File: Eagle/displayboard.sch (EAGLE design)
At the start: 47 parts

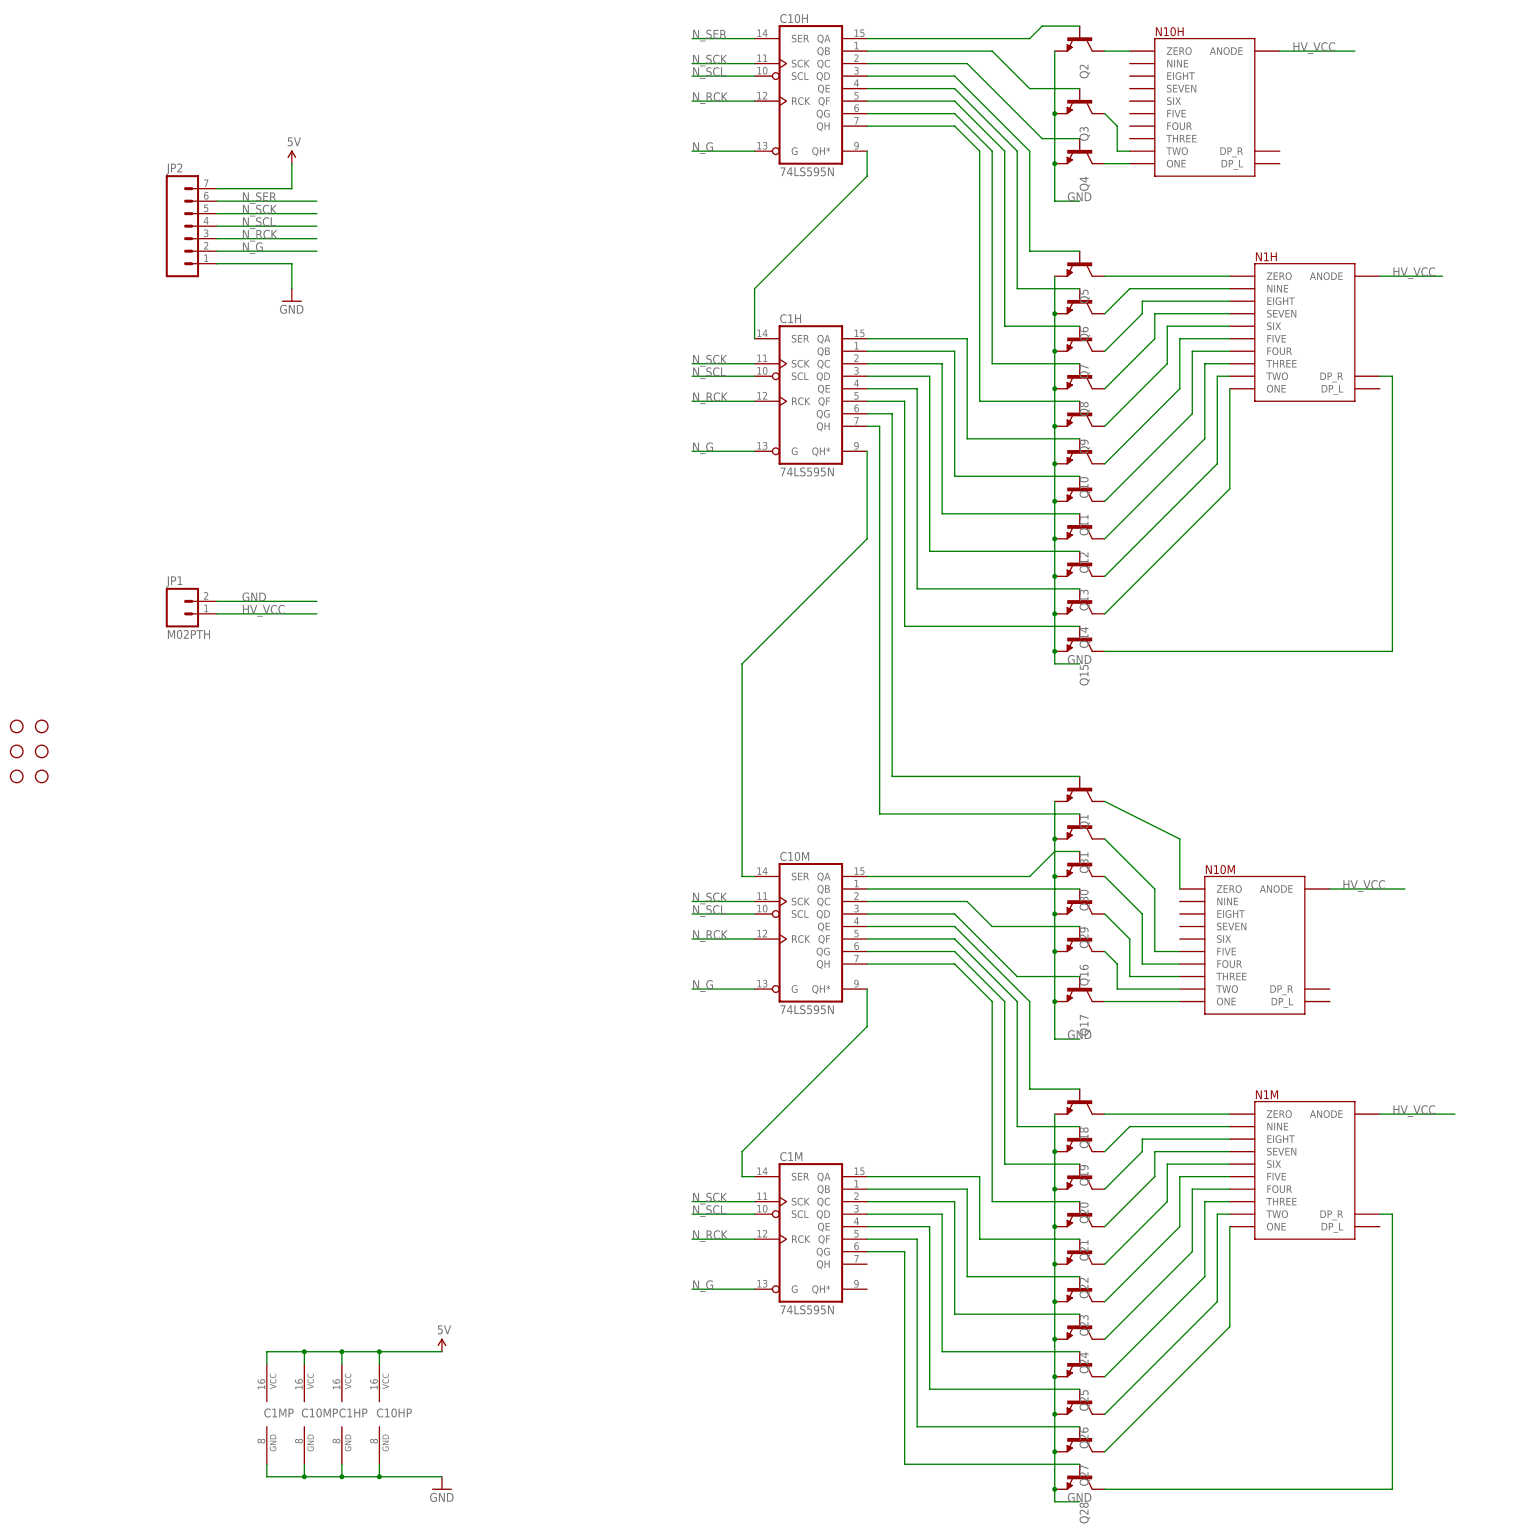
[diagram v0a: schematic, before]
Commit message: Update schematic to include on-board 200V psu
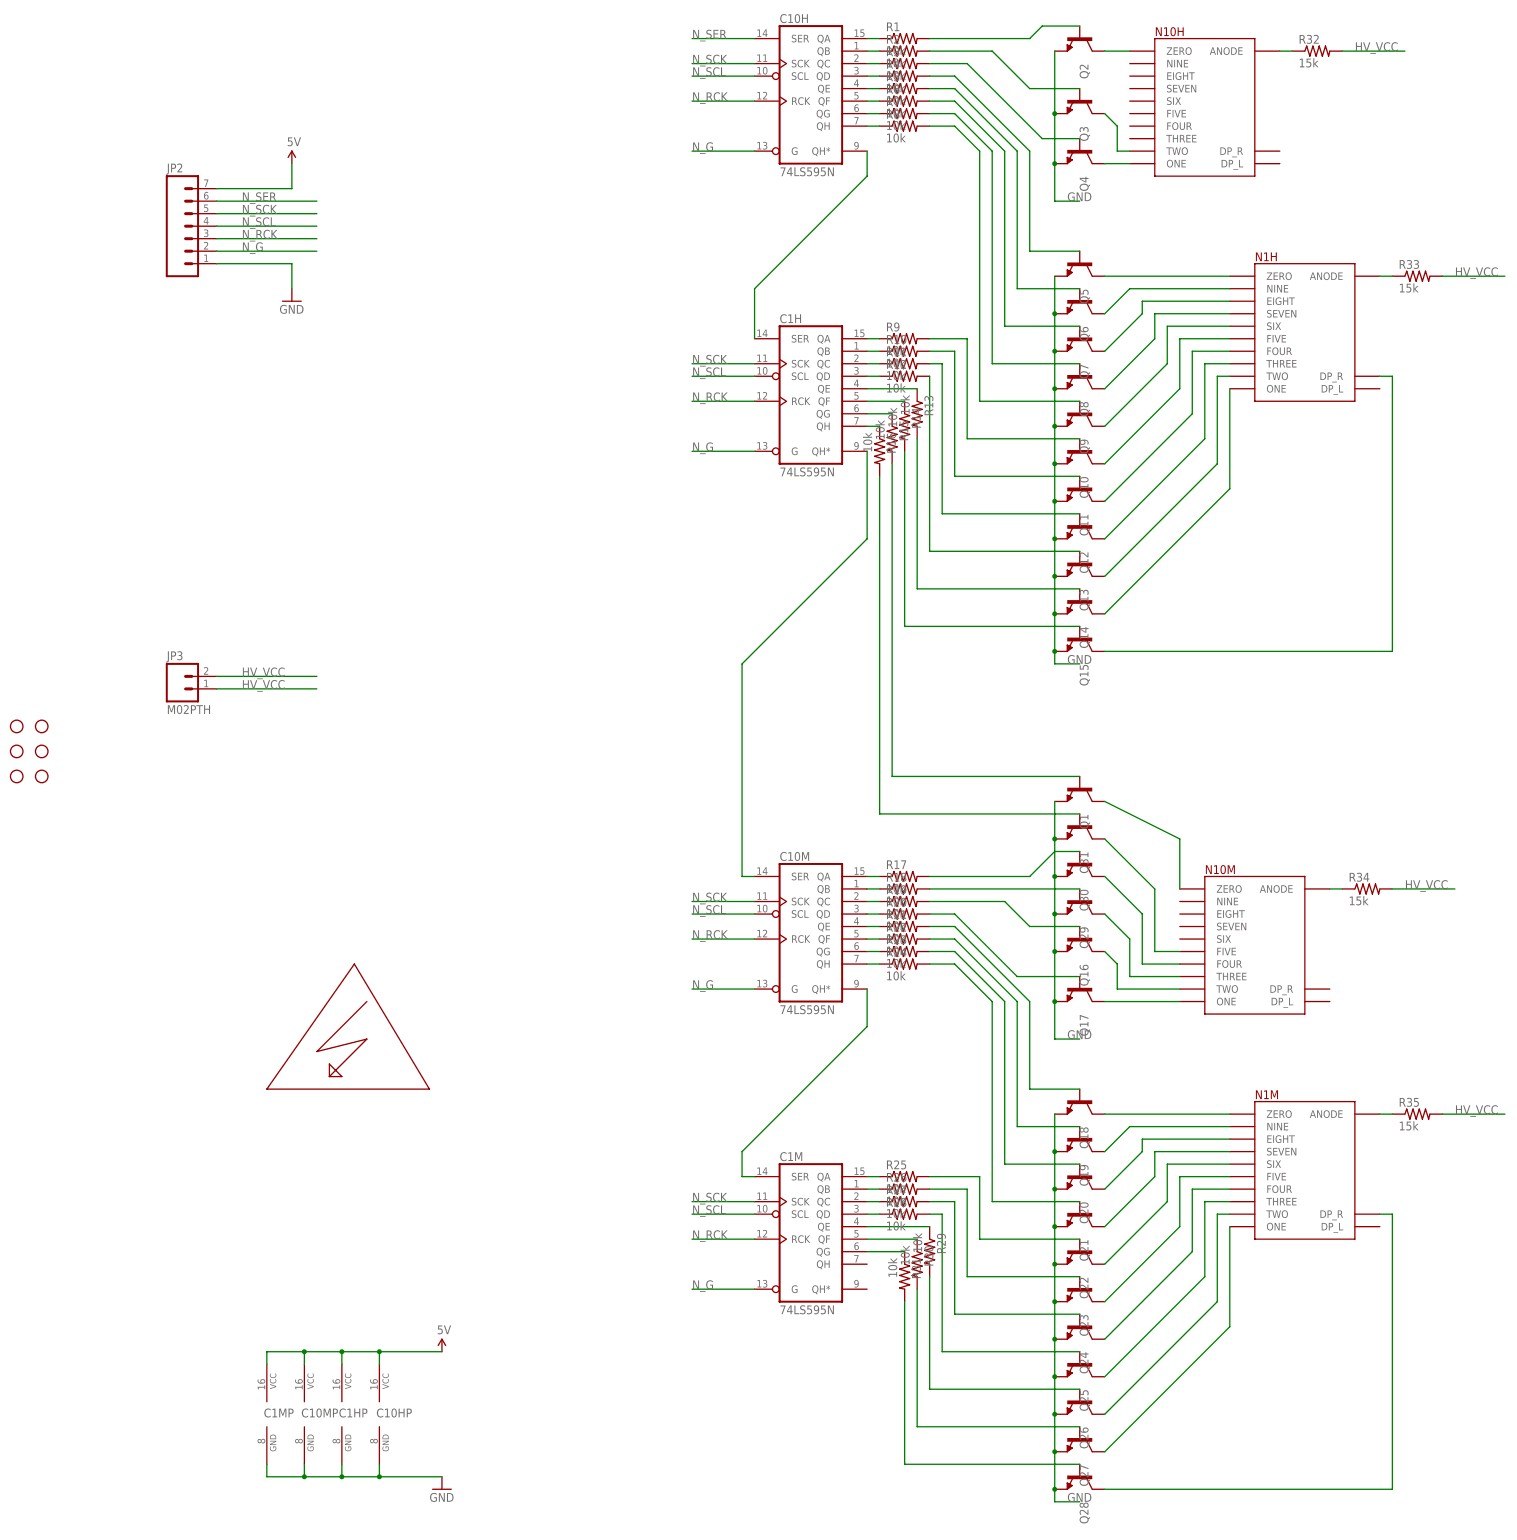
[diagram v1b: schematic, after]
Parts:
- removed JP1: M02PTH, SparkFun-Connectors:M02PTH
- added JP3: M02PTH, SparkFun-Connectors:M02PTH
- added R1, R10, R11, R12, R13, R14, R15, R16, R17, R18, R19, R2, R20, R21, R22, R23, R24, R25, R26, R27, R28, R29, R3, R30, R31, R4, R5, R6, R7, R8, R9: 10k, resistor:R-US_0204/7
- added R32, R33, R34, R35: 15k, resistor:R-US_0207/2V
- added U$1: HIGHVOLTAGE, highvoltage:HIGHVOLTAGE
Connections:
- new net N$100: N1H.ANODE, R33.1
- new net N$2: C10HA.QA, R1.1
- new net N$20: C10HA.QB, R2.1
- new net N$21: C10HA.QC, R3.1
- new net N$53: C10HA.QD, R4.1
- new net N$54: C10HA.QE, R5.1
- new net N$55: C10HA.QF, R6.1
- new net N$56: C10HA.QG, R7.1
- new net N$73: C10HA.QH, R8.1
- new net N$74: C1HA.QA, R9.1
- new net N$75: C1HA.QC, R11.1
- new net N$76: C1HA.QB, R10.1
- new net N$77: C1HA.QD, R12.1
- new net N$78: C1HA.QE, R13.1
- new net N$79: C1HA.QF, R14.1
- new net N$80: C1HA.QG, R15.1
- new net N$81: C1HA.QH, R16.1
- new net N$82: C10MA.QB, R18.1
- new net N$83: C10MA.QC, R19.1
- new net N$84: C10MA.QD, R20.1
- new net N$85: C10MA.QE, R21.1
- new net N$86: C10MA.QF, R22.1
- new net N$87: C10MA.QG, R23.1
- new net N$88: C10MA.QH, R24.1
- new net N$89: Q16.B, R19.2
- new net N$90: C1MA.QA, R25.1
- new net N$91: C1MA.QB, R26.1
- new net N$92: C1MA.QC, R27.1
- new net N$93: C1MA.QD, R28.1
- new net N$94: C1MA.QE, R29.1
- new net N$95: C1MA.QF, R30.1
- new net N$96: C1MA.QG, R31.1
- new net N$97: N10H.ANODE, R32.1
- new net N$98: N1M.ANODE, R35.1
- new net N$99: N10M.ANODE, R34.1
- net GND: no longer JP1.2
- net HV_VCC: now also JP3.1, JP3.2, R32.2, R33.2, R34.2, R35.2; no longer JP1.1, N10H.ANODE, N10M.ANODE, N1H.ANODE, N1M.ANODE
- net N$18: now also R1.2; no longer C10HA.QA
- net N$19: now also R2.2; no longer C10HA.QB
- net N$22: now also R3.2; no longer C10HA.QC
- net N$23: now also R4.2; no longer C10HA.QD
- net N$24: now also R5.2; no longer C10HA.QE
- net N$25: now also R6.2; no longer C10HA.QF
- net N$26: now also R7.2; no longer C10HA.QG
- net N$27: now also R8.2; no longer C10HA.QH
- net N$28: now also R9.2; no longer C1HA.QA
- net N$29: now also R10.2; no longer C1HA.QB
- net N$30: now also R11.2; no longer C1HA.QC
- net N$31: now also R12.2; no longer C1HA.QD
- net N$32: now also R13.2; no longer C1HA.QE
- net N$33: now also R14.2; no longer C1HA.QF
- net N$36: now also R15.2; no longer C1HA.QG
- net N$50: now also R17.2; no longer C10MA.QA
- net N$51: now also C10MA.QA, R17.1; no longer C10MA.QB, Q29.B
- net N$52: now also Q29.B, R18.2; no longer C10MA.QC, Q16.B
- net N$57: now also R25.2; no longer C1MA.QA
- net N$58: now also R26.2; no longer C1MA.QB
- net N$59: now also R27.2; no longer C1MA.QC
- net N$60: now also R28.2; no longer C1MA.QD
- net N$61: now also R29.2; no longer C1MA.QE
- net N$62: now also R30.2; no longer C1MA.QF
- net N$63: now also R31.2; no longer C1MA.QG
- net N$67: now also R16.2; no longer C1HA.QH
- net N$68: now also R20.2; no longer C10MA.QD
- net N$69: now also R23.2; no longer C10MA.QG
- net N$70: now also R21.2; no longer C10MA.QE
- net N$71: now also R22.2; no longer C10MA.QF
- net N$72: now also R24.2; no longer C10MA.QH
